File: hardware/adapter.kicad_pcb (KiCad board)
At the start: 2 copper layers, 0 parts

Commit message: hardware: 4-layer board, placement on both sides, J1 dimensioned
Takes the PCB from bare footprints to a fully placed 4-layer board. No
copper is routed yet and no zones are poured.

Stackup and outline
  Two inner copper layers added: In1.Cu intended as a solid ground plane
  directly beneath the component side, In2.Cu for power distribution. The
  board stays 62 x 68 mm. It is deliberately NOT grown: depth adds mass and
  lengthens the moment arm from the RJ45 cable back to the GPIB connector,
  and the mechanical load path is the connector's two M3 jackscrews on
  46.8 mm centres rather than its 24 signal contacts.

Placement
  All 90 footprints placed: 19 on F.Cu, 71 on B.Cu. Assembly is by hand, so
  back-side passives cost nothing and the 3D-printed enclosure accommodates
  them. Each decoupling capacitor sits on B.Cu directly beneath its IC's
  supply pin, so the connection is a through-via rather than a trace - the
  tightest supply loop available, and it costs no front-side area. That is
  what let the board stay 62 x 68 at ~35% front-side courtyard utilisation
  instead of the 68.7% a single-sided layout needed.

  Verified: zero courtyard overlaps; crystal load caps 0.00-4.00 mm from
  their crystals; C_U3a1 and C_U4a1 at 0.00 mm from their transceivers.

  Done with KiCad's own Flip() transform via the pcbnew Python API, one
  atomic pass, so pads, silkscreen, courtyards and 3D model offsets all
  moved correctly. auto_place_from_schematic was tried and rejected: it
  scored 15 -> 0, planned two parts to identical coordinates and put one
  off-board.

J1 GPIB connector
  Rotated 180 so the pad rows sit at the front edge and the shroud
  overhangs off-board, instead of the body consuming 24 mm of board depth.
  Set back so the two M3 mounting holes are 10.70 mm from the front edge
  per the mechanical drawing; hole span measures 46.80 mm, matching the
  datasheet. This costs 7.84 mm of board depth versus the earlier position
  and reduces the overhang to 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
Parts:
- added C6: 4u7, Capacitor_SMD:C_0805_2012Metric, B.Cu at (131.0, 92.0)
- added C7: 4u7, Capacitor_SMD:C_0805_2012Metric, B.Cu at (131.6, 94.4)
- added C_1V2O1: 10n, Capacitor_SMD:C_0805_2012Metric, B.Cu at (130.4, 89.6)
- added C_3V3: 1u, Capacitor_SMD:C_0805_2012Metric, B.Cu at (135.0, 92.0)
- added C_BIAS1: 100n, Capacitor_SMD:C_0805_2012Metric, B.Cu at (117.5, 122.6)
- added C_BULK1: 47u/16V, Capacitor_SMD:C_1206_3216Metric, B.Cu at (104.0, 123.0)
- added C_ETHa1: 100n, Capacitor_SMD:C_0805_2012Metric, B.Cu at (118.1, 125.0)
- added C_ETHb1: 100n, Capacitor_SMD:C_0805_2012Metric, B.Cu at (116.9, 120.2)
- added C_ETHbulk1: 10u, Capacitor_SMD:C_0805_2012Metric, B.Cu at (113.6, 123.6)
- added C_ETHc1: 100n, Capacitor_SMD:C_0805_2012Metric, B.Cu at (121.0, 119.1)
- added C_ETHd1: 100n, Capacitor_SMD:C_0805_2012Metric, B.Cu at (112.2, 121.2)
- added C_G1: 100n, Capacitor_SMD:C_0805_2012Metric, B.Cu at (150.0, 123.0)
- added C_LDOin1: 1u, Capacitor_SMD:C_0805_2012Metric, B.Cu at (105.5, 125.6)
- added C_LDOout1: 1u, Capacitor_SMD:C_0805_2012Metric, B.Cu at (103.2, 120.1)
- added C_RCT1: 22n, Capacitor_SMD:C_0805_2012Metric, B.Cu at (116.9, 98.8)
- added C_SH1: 1n, Capacitor_SMD:C_0805_2012Metric, B.Cu at (144.0, 77.2)
- added C_TCT1: 22n, Capacitor_SMD:C_0805_2012Metric, B.Cu at (122.1, 98.8)
- added C_TOCAP1: 4u7, Capacitor_SMD:C_0805_2012Metric, B.Cu at (109.8, 124.7)
- added C_U3a1: 100n, Capacitor_SMD:C_0805_2012Metric, B.Cu at (114.0, 93.0)
- added C_U3b1: 4u7, Capacitor_SMD:C_0805_2012Metric, B.Cu at (114.6, 95.4)
- added C_U4a1: 100n, Capacitor_SMD:C_0805_2012Metric, B.Cu at (148.0, 93.0)
- added C_U4b1: 4u7, Capacitor_SMD:C_0805_2012Metric, B.Cu at (148.6, 95.4)
- added C_VDD1: 100n, Capacitor_SMD:C_0805_2012Metric, B.Cu at (110.6, 118.6)
- added C_X1a1: 15p, Capacitor_SMD:C_0805_2012Metric, B.Cu at (131.0, 84.0)
- added C_X1b1: 15p, Capacitor_SMD:C_0805_2012Metric, B.Cu at (131.6, 86.4)
- added C_X2a1: 18p, Capacitor_SMD:C_0805_2012Metric, B.Cu at (125.7, 124.3)
- added C_X2b1: 18p, Capacitor_SMD:C_0805_2012Metric, B.Cu at (125.0, 121.9)
- added D_BR1: MB6S-TP, adapter:MBS_L4.7-W4.0-P2.50-LS7.0-TL, F.Cu at (127.0, 119.5)
- added D_BR2: MB6S-TP, adapter:MBS_L4.7-W4.0-P2.50-LS7.0-TL, F.Cu at (131.5, 123.0)
- added J1: 112-024-113R001, adapter:CONN_112-024-113R001_NRC, F.Cu at (142.9, 72.8)
- added J2: DGUK411Q211DB2A1DP2, adapter:RJ45-TH_DGUK411Q211DB2A1DP2, F.Cu at (119.5, 108.5)
- added J3: USB-C, adapter:USB-C_SMD-TYPE-C-31-M-12_1, F.Cu at (141.0, 122.0)
- added L1: 3u3, Inductor_SMD:L_0805_2012Metric, F.Cu at (138.0, 90.0)
- added L2: HH-1M1608-121JT, Inductor_SMD:L_0603_1608Metric, F.Cu at (108.0, 118.0)
- added LED1: green, LED_SMD:LED_0805_2012Metric, F.Cu at (150.2, 119.7)
- added M1: DP9900LPB-5V1.4A, adapter:COMM-SMD_DP9900LPB-5V1.4A, F.Cu at (147.0, 107.0)
- added Q1: AO3401A, Package_TO_SOT_SMD:SOT-23, F.Cu at (150.0, 123.0)
- added Q2: 2N7002, Package_TO_SOT_SMD:SOT-23, F.Cu at (155.0, 123.0)
- added RSET1: 12k4, Resistor_SMD:R_0805_2012Metric, B.Cu at (124.9, 118.3)
- added R_ATN1: 10k, Resistor_SMD:R_0805_2012Metric, B.Cu at (147.4, 90.6)
- added R_B1: 10R, Resistor_SMD:R_0805_2012Metric, B.Cu at (119.5, 96.0)
- added R_CC1: 5k1, Resistor_SMD:R_0805_2012Metric, B.Cu at (140.0, 118.1)
- added R_CC2: 5k1, Resistor_SMD:R_0805_2012Metric, B.Cu at (144.9, 118.1)
- added R_CFG1: 10k, Resistor_SMD:R_0805_2012Metric, B.Cu at (127.1, 93.0)
- added R_DC1: 10k, Resistor_SMD:R_0805_2012Metric, B.Cu at (152.0, 93.0)
- added R_G1: 100k, Resistor_SMD:R_0805_2012Metric, B.Cu at (150.6, 125.4)
- added R_G2: 100k, Resistor_SMD:R_0805_2012Metric, B.Cu at (154.0, 123.0)
- added R_IFC1: 10k, Resistor_SMD:R_0805_2012Metric, B.Cu at (144.1, 94.0)
- added R_INTP1: 4k7, Resistor_SMD:R_0805_2012Metric, B.Cu at (129.1, 119.5)
- added R_LED1: 1k, Resistor_SMD:R_0805_2012Metric, B.Cu at (150.2, 119.7)
- added R_LEDL1: 330, Resistor_SMD:R_0805_2012Metric, B.Cu at (126.0, 97.2)
- added R_LEDR1: 330, Resistor_SMD:R_0805_2012Metric, B.Cu at (110.0, 99.0)
- added R_PE1: 0R, Resistor_SMD:R_0805_2012Metric, B.Cu at (113.4, 90.6)
- added R_REN1: 10k, Resistor_SMD:R_0805_2012Metric, B.Cu at (151.2, 89.8)
- added R_RSTP1: 4k7, Resistor_SMD:R_0805_2012Metric, B.Cu at (133.5, 122.6)
- added R_RUN1: 10k, Resistor_SMD:R_0805_2012Metric, B.Cu at (134.2, 88.8)
- added R_RX1: 3R3, Resistor_SMD:R_0805_2012Metric, B.Cu at (119.5, 93.5)
- added R_RX2: 3R3, Resistor_SMD:R_0805_2012Metric, B.Cu at (130.1, 97.9)
- added R_SH1: 0R, Resistor_SMD:R_0805_2012Metric, B.Cu at (141.2, 79.9)
- added R_SRQ1: 10k, Resistor_SMD:R_0805_2012Metric, B.Cu at (149.3, 97.8)
- added R_T1: 49R9, Resistor_SMD:R_0805_2012Metric, B.Cu at (135.0, 108.5)
- added R_T2: 49R9, Resistor_SMD:R_0805_2012Metric, B.Cu at (135.0, 112.6)
- added R_T3: 49R9, Resistor_SMD:R_0805_2012Metric, B.Cu at (135.0, 104.4)
- added R_T4: 49R9, Resistor_SMD:R_0805_2012Metric, B.Cu at (107.5, 96.5)
- added R_TE1: 10k, Resistor_SMD:R_0805_2012Metric, B.Cu at (144.5, 96.5)
- added R_TX1: 3R3, Resistor_SMD:R_0805_2012Metric, B.Cu at (119.5, 91.0)
- added R_TX2: 3R3, Resistor_SMD:R_0805_2012Metric, B.Cu at (135.1, 117.5)
- added R_XF1: 1M, Resistor_SMD:R_0805_2012Metric, B.Cu at (129.7, 124.3)
- added TP_3V3: TP_3V3, TestPoint:TestPoint_Pad_D1.5mm, B.Cu at (117.0, 64.0)
- added TP_5V1: TP_5V, TestPoint:TestPoint_Pad_D1.5mm, B.Cu at (119.6, 64.0)
- added TP_ATN1: TP_ATN, TestPoint:TestPoint_Pad_D1.5mm, B.Cu at (134.8, 64.0)
- added TP_DAV1: TP_DAV, TestPoint:TestPoint_Pad_D1.5mm, B.Cu at (147.5, 64.0)
- added TP_DC1: TP_DC, TestPoint:TestPoint_Pad_D1.5mm, B.Cu at (132.3, 64.0)
- added TP_GND1: TP_GND, TestPoint:TestPoint_Pad_D1.5mm, B.Cu at (114.5, 64.0)
- added TP_GPIO221: TP_GPIO22, TestPoint:TestPoint_Pad_D1.5mm, B.Cu at (127.2, 64.0)
- added TP_IFC1: TP_IFC, TestPoint:TestPoint_Pad_D1.5mm, B.Cu at (139.9, 64.0)
- added TP_NDAC1: TP_NDAC, TestPoint:TestPoint_Pad_D1.5mm, B.Cu at (142.4, 64.0)
- added TP_NRFD1: TP_NRFD, TestPoint:TestPoint_Pad_D1.5mm, B.Cu at (145.0, 64.0)
- added TP_SRQ1: TP_SRQ, TestPoint:TestPoint_Pad_D1.5mm, B.Cu at (137.4, 64.0)
- added TP_SWCLK1: TP_SWCLK, TestPoint:TestPoint_Pad_D1.5mm, B.Cu at (122.1, 64.0)
- added TP_SWDIO1: TP_SWDIO, TestPoint:TestPoint_Pad_D1.5mm, B.Cu at (124.7, 64.0)
- added TP_TE1: TP_TE, TestPoint:TestPoint_Pad_D1.5mm, B.Cu at (129.7, 64.0)
- added U1: RP2354A, adapter:QFN-60_L7.0-W7.0-P0.40-TL-EP3.4, F.Cu at (131.0, 92.0)
- added U2: W5500, Package_QFP:LQFP-48_7x7mm_P0.5mm, F.Cu at (117.5, 122.6)
- added U3: SN75160BDW, Package_SO:SOIC-20W_7.5x12.8mm_P1.27mm, F.Cu at (112.0, 83.0)
- added U4: SN75161BDW, Package_SO:SOIC-20W_7.5x12.8mm_P1.27mm, F.Cu at (148.0, 93.0)
- added U5: AP2114H-3.3TRG1, adapter:SOT-223_L6.7-W3.5-P2.30-BR, F.Cu at (104.0, 123.0)
- added U6: TPS3839G33DBZR, Package_TO_SOT_SMD:SOT-23, F.Cu at (110.0, 123.0)
- added X1: 12MHz, Crystal:Crystal_SMD_3225-4Pin_3.2x2.5mm, F.Cu at (131.0, 84.0)
- added X2: 25MHz, Crystal:Crystal_SMD_3225-4Pin_3.2x2.5mm, F.Cu at (125.7, 124.3)
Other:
- board outline added: 62 x 68 mm
- copper layers 2 -> 4
- board text added: "3V3"
- board text added: "5V"
- board text added: "ATN"
- board text added: "DAV"
- board text added: "DC"
- board text added: "GND"
- board text added: "GP22"
- board text added: "IFC"
- board text added: "NDAC"
- board text added: "NRFD"
- board text added: "SRQ"
- board text added: "SWCLK"
- board text added: "SWDIO"
- board text added: "TE"

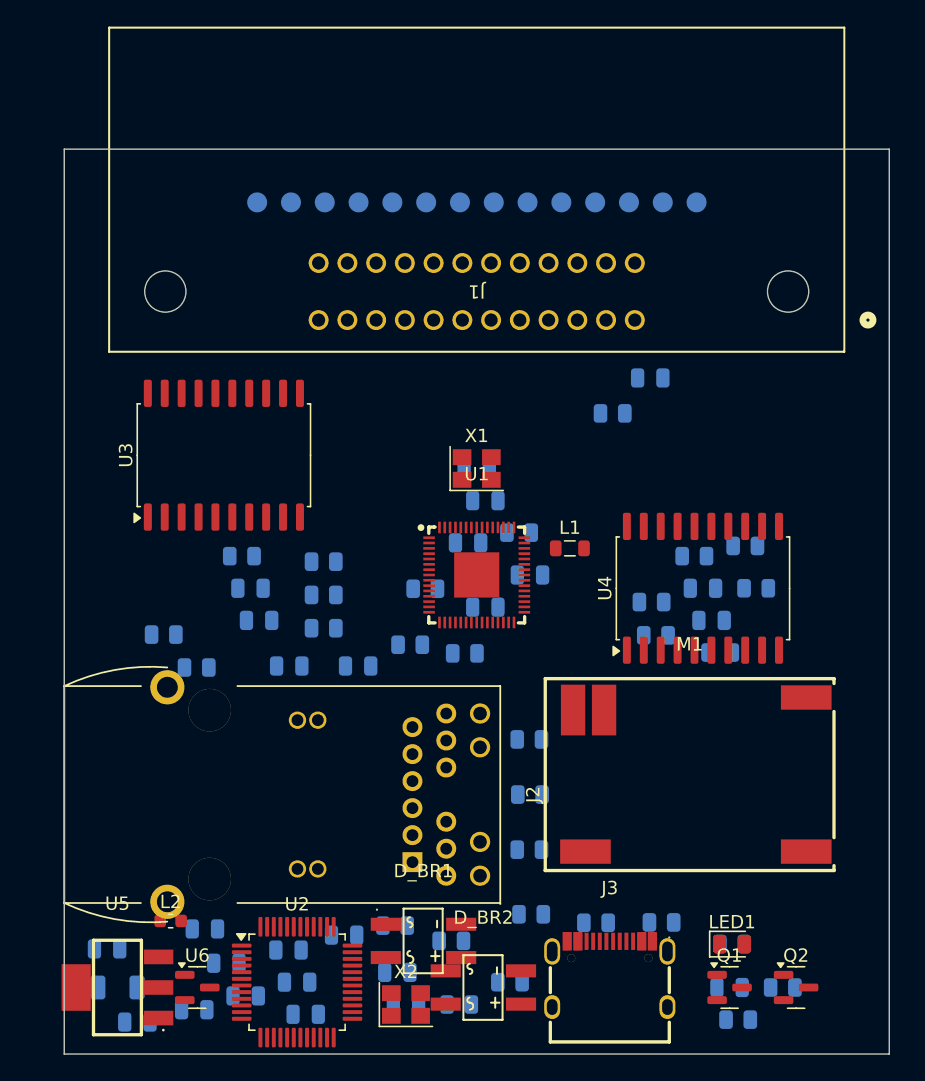
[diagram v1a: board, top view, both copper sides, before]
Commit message: hardware: USB-C alternate power source, J2 swapped to HanRun HR871150C
Implements the USB-C-as-alternative-power-source design (design-spec
§30.1): a 1x3 2.54mm header (J4) selects the system rail source via a
jumper rather than a diode-OR, since a Schottky drop would put +5V_SYS
below the SN75160B/161B's 4.75V minimum. Pin 1 = +5V_POE (M1's isolated
output), pin 2 = +5V_SYS (everything downstream), pin 3 = VBUS (from
J3's USB-C pads, already present with 5k1 CC pull-downs). R_G1/C_G1 stay
referenced to +5V_SYS along with Q1's source (R-HW-020): the gate
pull-up must track whichever rail the source actually sits on, or Q1
turns on with IOVDD absent whenever the other source is unpowered.

J2 (PoE RJ45) swapped from a generic MagJack footprint to the actual
ordered part, HanRun HR871150C (LCSC C19724786), correcting the PoE tap
pin numbers (J2.7-10, was J2.13-16) and the shield/ground pin scheme
against its real datasheet pinout.

Added docs/rp2354a-pinmap.md (RP2354A pin assignments) and
hardware/adapter.kicad_dru (project DRC rules). netlist-check.py's
bias-rail-discipline check extended to also flag +5V_SYS, matching the
new rail.
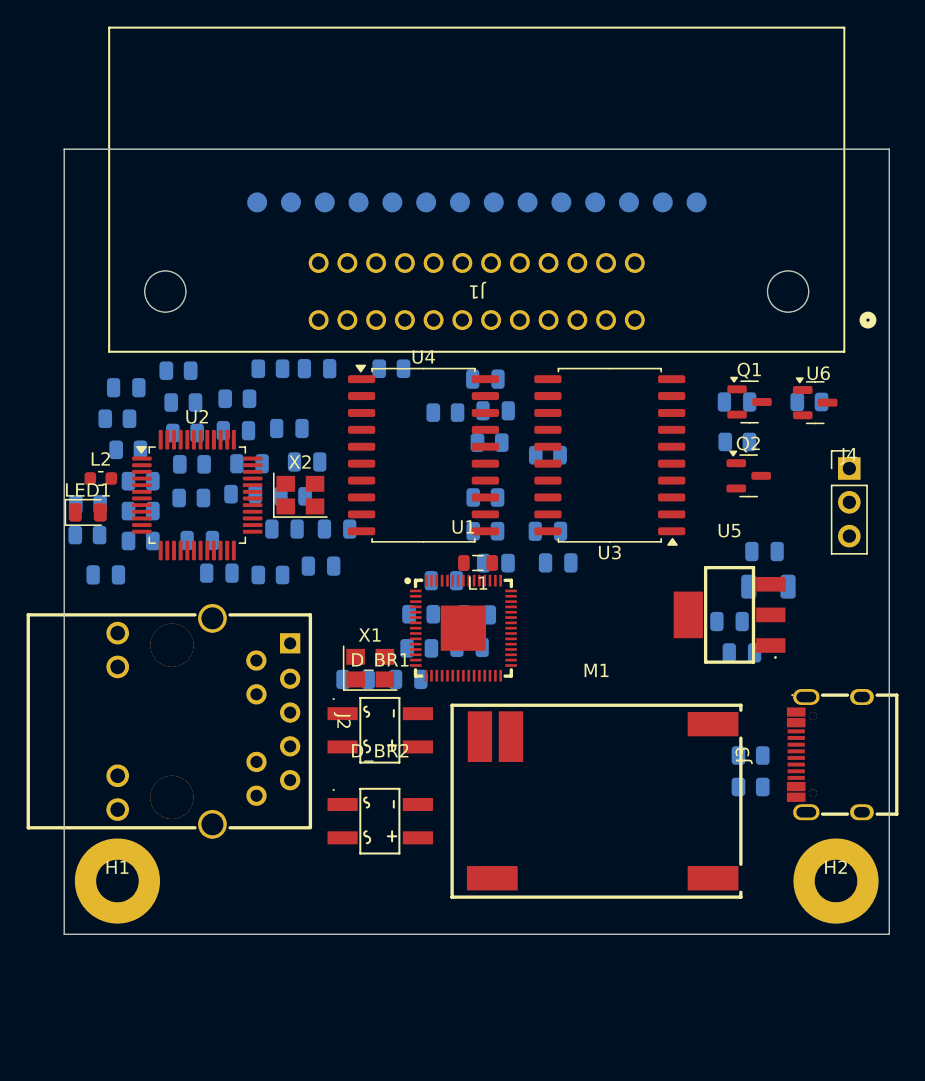
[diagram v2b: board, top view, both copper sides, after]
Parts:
- removed C_TCT1: 22n, Capacitor_SMD:C_0805_2012Metric
- added H1: MountingHole_Pad, MountingHole:MountingHole_3.2mm_M3_Pad, F.Cu at (104.0, 115.0)
- added H2: MountingHole_Pad, MountingHole:MountingHole_3.2mm_M3_Pad, F.Cu at (158.0, 115.0)
- added J4: PWR_SEL, Connector_PinHeader_2.54mm:PinHeader_1x03_P2.54mm_Vertical, F.Cu at (159.0, 84.0)
- J2: value DGUK411Q211DB2A1DP2 -> HR871150C; footprint adapter:RJ45-TH_DGUK411Q211DB2A1DP2 -> adapter:RJ45-TH_HR871150C
- moved U6 63.9 mm to (156.4, 79.0)
- moved C_LDOin1 58.9 mm to (152.6, 90.2)
- moved LED1 58.3 mm to (101.8, 87.3)
- moved C_BULK1 57.4 mm to (152.9, 92.9)
- moved R_LED1 57.4 mm to (101.7, 89.0)
- moved U5 53.9 mm to (150.0, 95.0)
- moved C_LDOout1 52.6 mm to (150.9, 97.8)
- moved R_TX2 48.5 mm to (104.0, 80.3)
- moved R_RSTP1 48.4 mm to (113.0, 78.8)
- moved R_INTP1 45.2 mm to (109.0, 79.0)
- moved R_G2 44.0 mm to (156.0, 79.0)
- moved Q1 44.0 mm to (151.5, 79.0)
- moved C_G1 44.0 mm to (150.6, 79.0)
- moved C_ETHb1 44.0 mm to (104.7, 77.9)
- moved R_G1 43.4 mm to (150.6, 82.0)
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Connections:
- C_BULK1 pad 1: +5V_POE -> +5V_SYS
- C_G1 pad 1: +5V_POE -> +5V_SYS
- C_LDOin1 pad 1: +5V_POE -> +5V_SYS
- J2 pad 1: unconnected-(J2-CT-Pad1) -> /Ethernet W5500 and magjack/ETH_TXP
- J2 pad 10: /Ethernet W5500 and magjack/ETH_TXN -> /Ethernet W5500 and magjack/POE_TAP_B2
- J2 pad 11: /Ethernet W5500 and magjack/ETH_TXP -> /Ethernet W5500 and magjack/ETH_LEDL_A
- J2 pad 12: /Ethernet W5500 and magjack/ETH_TCT -> /Ethernet W5500 and magjack/ETH_LINKLED
- J2 pad 13: /Ethernet W5500 and magjack/POE_TAP_A1 -> /Ethernet W5500 and magjack/ETH_LEDR_A
- J2 pad 14: /Ethernet W5500 and magjack/POE_TAP_A2 -> /Ethernet W5500 and magjack/ETH_ACTLED
- J2 pad 15: /Ethernet W5500 and magjack/POE_TAP_B1 -> GND
- J2 pad 16: /Ethernet W5500 and magjack/POE_TAP_B2 -> GND
- J2 pad 2: unconnected-(J2-TD3--Pad2) -> /Ethernet W5500 and magjack/ETH_TXN
- J2 pad 3: unconnected-(J2-TD3+-Pad3) -> /Ethernet W5500 and magjack/ETH_RCT
- J2 pad 7: unconnected-(J2-CT-Pad7) -> /Ethernet W5500 and magjack/POE_TAP_A1
- J2 pad 8: unconnected-(J2-TD4+-Pad8) -> /Ethernet W5500 and magjack/POE_TAP_A2
- J2 pad 9: unconnected-(J2-TD4--Pad9) -> /Ethernet W5500 and magjack/POE_TAP_B1
- J3 pad A4B9: unconnected-(J3-VBUS-PadA4B9) -> VBUS
- J3 pad B4A9: unconnected-(J3-VBUS-PadB4A9) -> VBUS
- Q1 pad 2: +5V_POE -> +5V_SYS
- R_G1 pad 1: +5V_POE -> +5V_SYS
- TP_5V1 pad 1: +5V_POE -> +5V_SYS
- U5 pad 3: +5V_POE -> +5V_SYS
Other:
- board size 62 x 68 mm -> 62 x 59 mm
